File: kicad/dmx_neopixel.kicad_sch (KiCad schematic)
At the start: 30 parts, among them J1 USB_C_Receptacle_USB2.0_16P, J2 NC3MAH, J3 NC3FAH2, J4 Conn_01x03_Pin, J7 Jack-DC, Q1 BSS138, SW1 SW_DIP_x10, U1 ESP32-S3-WROOM-1, U2 MAX3485, U3 AP7333-33SA, U4 BP5293-50

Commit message: feat: v0.2の基板を作成
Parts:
- removed J4: Conn_01x03_Pin, Connector_JST:JST_XH_B3B-XH-A_1x03_P2.50mm_Vertical, symbol Connector:Conn_01x03_Pin
- added J5: Conn_01x02_Pin, Connector_JST:JST_XH_B2B-XH-A_1x02_P2.50mm_Vertical, symbol Connector:Conn_01x02_Pin
- added SW2: SW_Push, Button_Switch_SMD:SW_SPST_PTS810, symbol Switch:SW_Push
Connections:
- net DMX_D-: now also SW1.10; no longer SW1.1
- net GND: now also SW1.20, J5.2 (Pin_2), SW2.2; no longer SW1.11
- net SW_2: now also U1.34 (IO41); no longer U1.38 (IO2)
- net SW_3: now also U1.33 (IO40); no longer U1.15 (IO3)
- net SW_4: now also U1.32 (IO39); no longer U1.4 (IO4)
- net SW_5: now also U1.31 (IO38); no longer U1.5 (IO5)
- net SW_6: now also U1.17 (IO9); no longer U1.6 (IO6)
- net SW_7: now also U1.18 (IO10); no longer U1.7 (IO7)
- net SW_8: now also U1.19 (IO11); no longer U1.12 (IO8)
- net SW_9: now also U1.20 (IO12); no longer U1.17 (IO9)
- net LED_DATA: now reaches U1.21 (IO13)
- net LED_DATA: now also Q1.2 (S), R3.2
- net SW_MODE: now reaches U1.22 (IO14)
- net SW_MODE: now also SW2.1
- net SW_1: now reaches U1.35 (IO42)
- net SW_1: now also SW1.1
- net at D3.1 (DOUT): now also J5.1 (Pin_1)
- net at R5.1: now also SW1.11; no longer SW1.20
- removed net LED_DIN: Q1.2 (S), R3.2, U1.39 (IO1)
- removed net SW_10: SW1.10, U1.18 (IO10)
- no-connect marks 4 -> 3
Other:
- moved on the sheet: R5

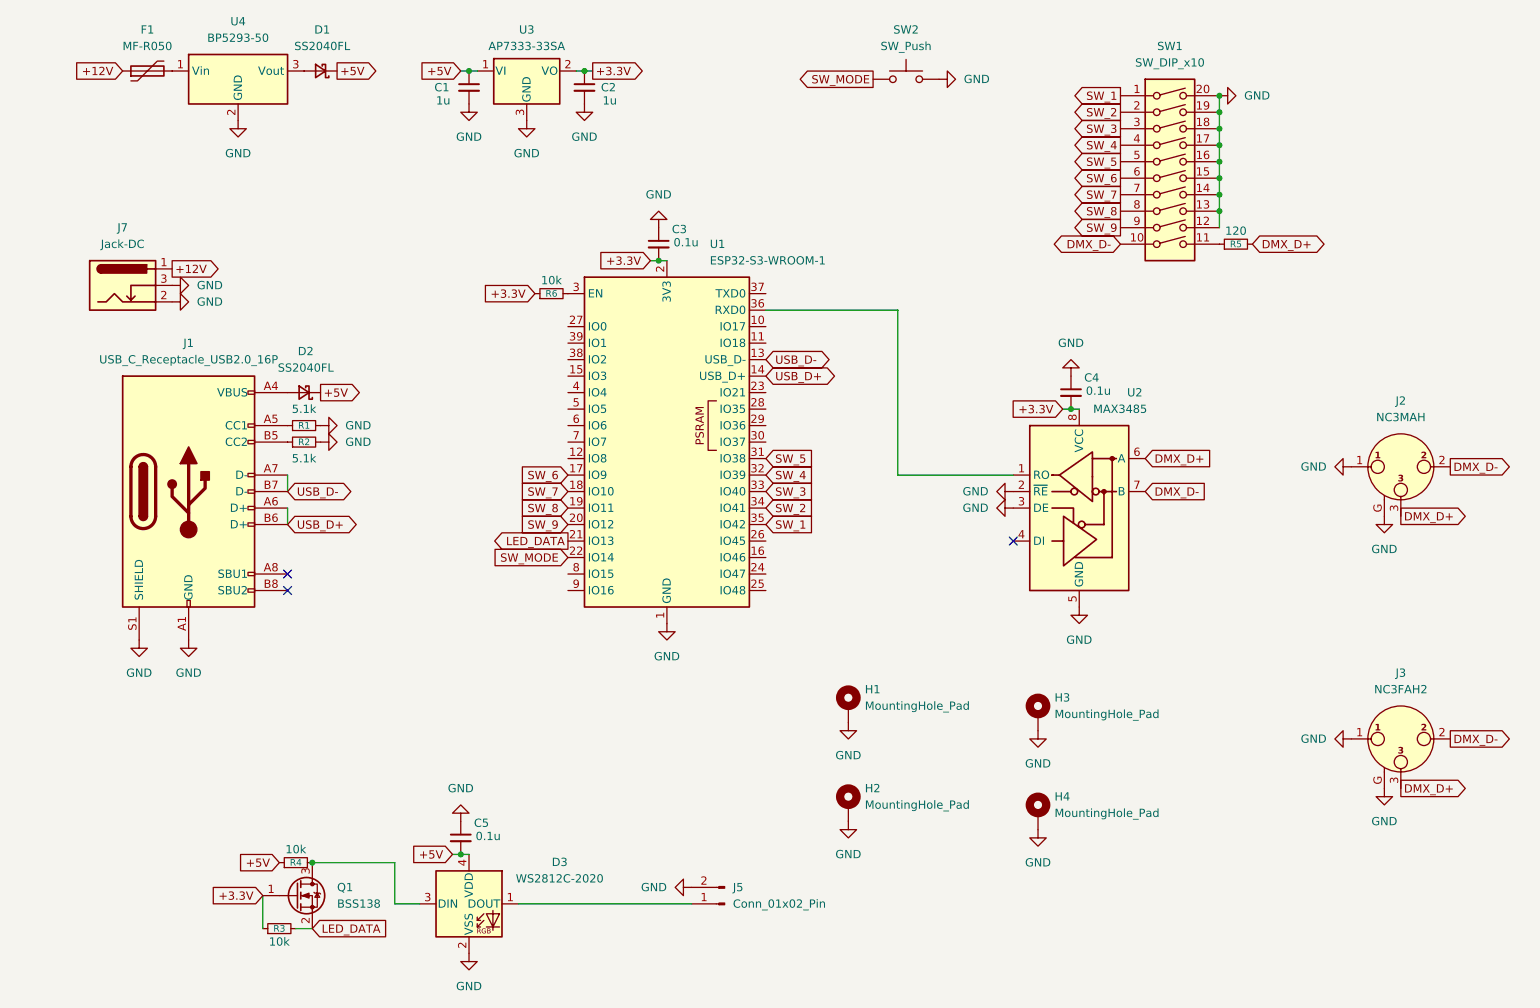
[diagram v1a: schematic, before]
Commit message: feat: ESP32をC3に変更
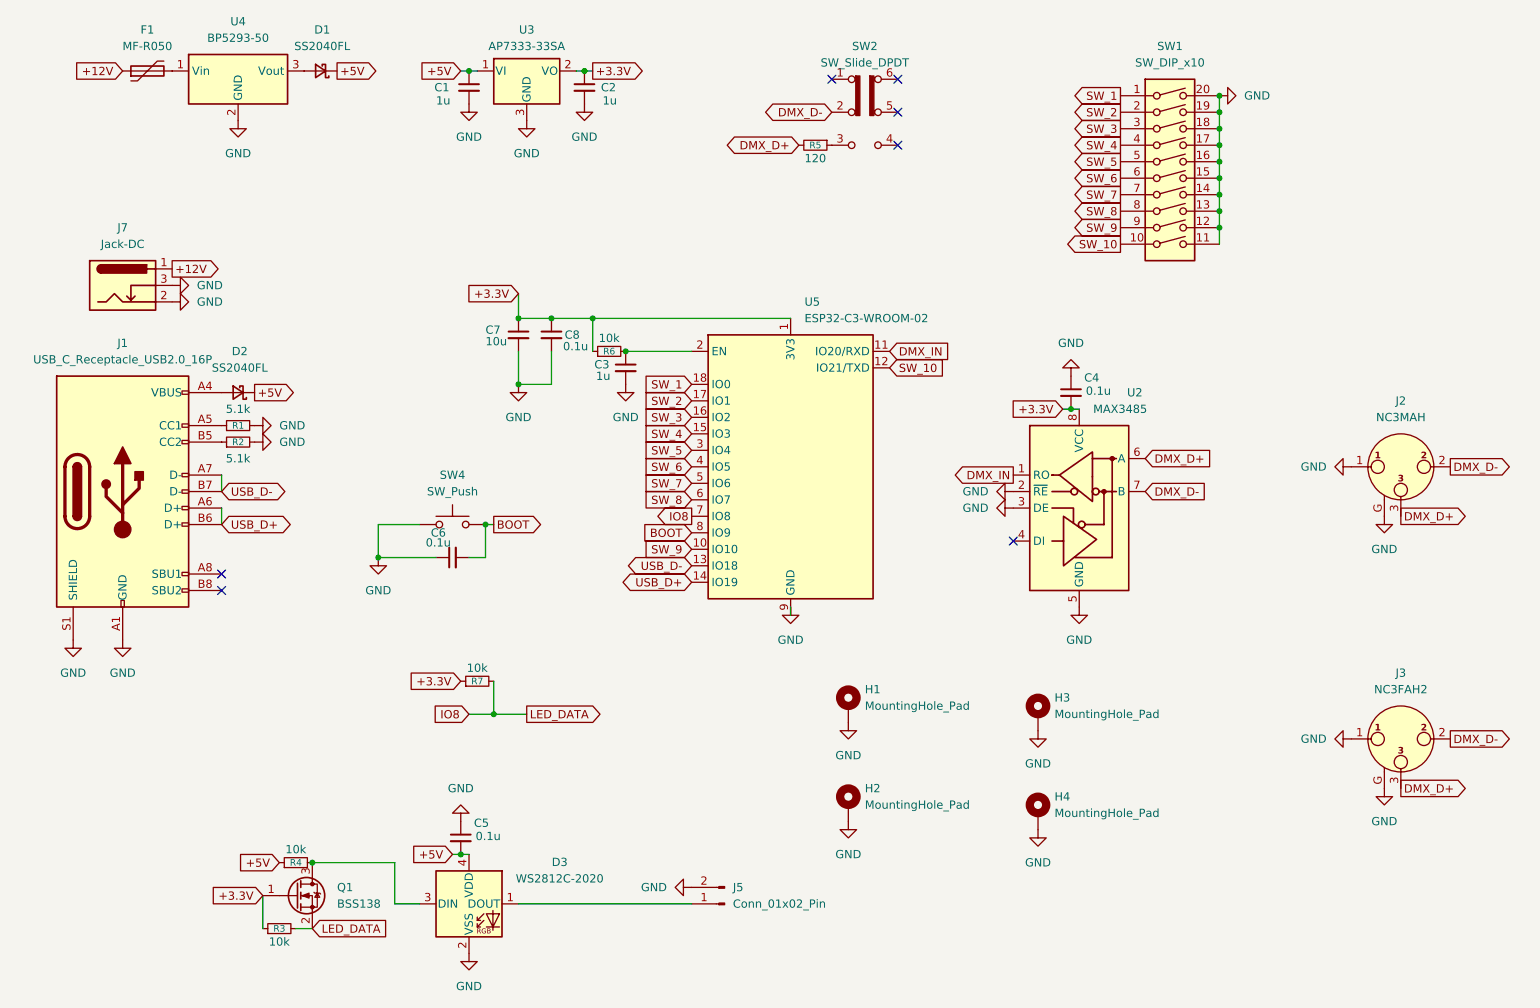
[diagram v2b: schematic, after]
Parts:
- removed SW2: SW_Push, Button_Switch_SMD:SW_SPST_PTS810, symbol Switch:SW_Push
- removed U1: ESP32-S3-WROOM-1, RF_Module:ESP32-S3-WROOM-1, symbol RF_Module:ESP32-S3-WROOM-1
- added C6, C8: 0.1u, Capacitor_SMD:C_0603_1608Metric_Pad1.08x0.95mm_HandSolder, symbol Device:C_Small
- added C7: 10u, Capacitor_SMD:C_0603_1608Metric_Pad1.08x0.95mm_HandSolder, symbol Device:C_Small
- added R7: 10k, Resistor_SMD:R_0603_1608Metric_Pad0.98x0.95mm_HandSolder, symbol Device:R_Small
- added SW2: SW_Slide_DPDT, Button_Switch_SMD:SW_DPDT_CK_JS202011JCQN, symbol Switch:SW_Slide_DPDT
- added SW4: SW_Push, Button_Switch_SMD:SW_SPST_PTS810, symbol Switch:SW_Push
- added U5: ESP32-C3-WROOM-02, RF_Module:ESP32-C3-WROOM-02, symbol RF_Module:ESP32-C3-WROOM-02
- C3: value 0.1u -> 1u
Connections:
- net +3.3V: now also C7.1, C8.1, R7.1, U5.1 (3V3); no longer C3.2
- net DMX_D-: now also SW2.2 (B); no longer SW1.10
- net GND: now also C3.2, SW1.11, C6.1, C7.2, C8.2, SW4.1, U5.19 (GND), U5.9 (GND); no longer C3.1
- net SW_1: now also U5.18 (IO0)
- net SW_2: now also U5.17 (IO1)
- net SW_3: now also U5.16 (IO2)
- net SW_4: now also U5.15 (IO3)
- net SW_5: now also U5.3 (IO4)
- net SW_6: now also U5.4 (IO5)
- net SW_7: now also U5.5 (IO6)
- net SW_8: now also U5.6 (IO7)
- net SW_9: now also U5.10 (IO10)
- net USB_D+: now also U5.14 (IO19)
- net USB_D-: now also U5.13 (IO18)
- net at R6.2: now also C3.1, U5.2 (EN)
- net DMX_IN: now reaches U2.1 (RO)
- net DMX_IN: now also U5.11 (IO20/RXD)
- net at R5.1: now also SW2.3 (C); no longer SW1.11
- net LED_DATA renamed IO8
- net IO8: now also R7.2, U5.7 (IO8)
- new net BOOT: C6.2, SW4.2, U5.8 (IO9)
- new net SW_10: SW1.10, U5.12 (IO21/TXD)
- no-connect marks 3 -> 7
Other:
- moved on the sheet: D2, J1, R1, R2, R5, R6

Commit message: feat: v1.0の基板データを追加
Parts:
- removed R5: 120, Resistor_SMD:R_0603_1608Metric_Pad0.98x0.95mm_HandSolder, symbol Device:R_Small
- removed R7: 10k, Resistor_SMD:R_0603_1608Metric_Pad0.98x0.95mm_HandSolder, symbol Device:R_Small
- removed SW2: SW_Slide_DPDT, Button_Switch_SMD:SW_DPDT_CK_JS202011JCQN, symbol Switch:SW_Slide_DPDT
- J3: renamed from J5; footprint Connector_JST:JST_XH_B2B-XH-A_1x02_P2.50mm_Vertical -> Connector_JST:JST_XH_S2B-XH-A_1x02_P2.50mm_Horizontal
- SW1: renamed from SW4; footprint Button_Switch_SMD:SW_SPST_PTS810 -> Button_Switch_SMD:SW_SPST_B3U-1000P
- renumbered C6 to C1, C5 to C2, C1 to C3, C7 to C4, C8 to C5, C2 to C6, C3 to C7, C4 to C8, D2 to D1, D1 to D2, J7 to J1, J1 to J2, J2 to J4, J3 to J5, R6 to R5, SW1 to SW2, U4 to U1, U3 to U2, U5 to U3, U2 to U4
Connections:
- net IO8 renamed LED_DATA
- no-connect marks 7 -> 3

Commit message: feat: 基板データ更新
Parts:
- SW1: footprint Button_Switch_SMD:SW_SPST_B3U-1000P -> Button_Switch_SMD:SW_SPST_PTS810
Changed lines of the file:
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@@
 			)
 		)
-		(property "Footprint" "Button_Switch_SMD:SW_SPST_B3U-1000P"
+		(property "Footprint" "Button_Switch_SMD:SW_SPST_PTS810"
 			(at 91.44 102.87 0)
 			(effects
